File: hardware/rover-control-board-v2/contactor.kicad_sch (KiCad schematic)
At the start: 10 parts, among them Q1 Q_NMOS_DGS

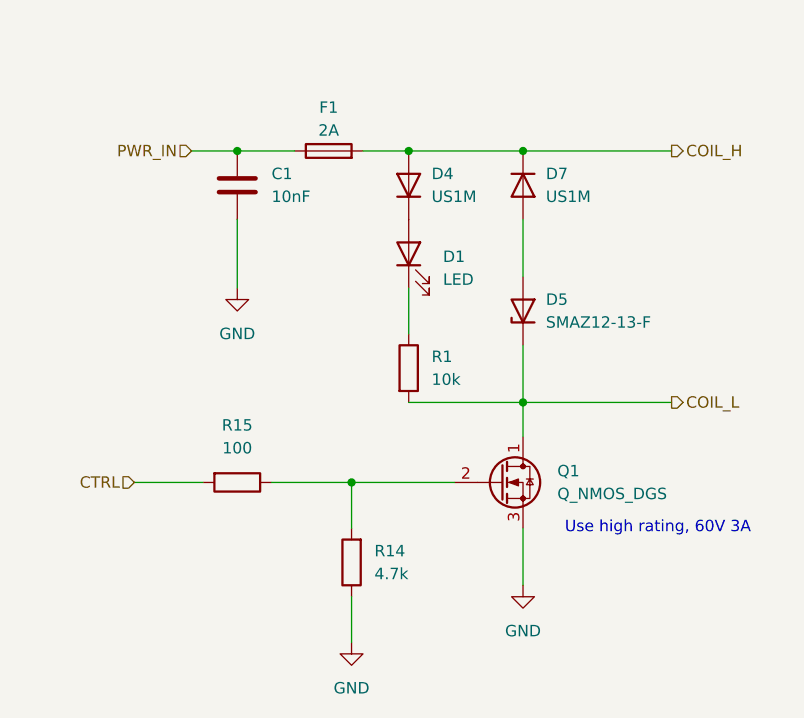
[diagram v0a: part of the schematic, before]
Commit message: Bus routed
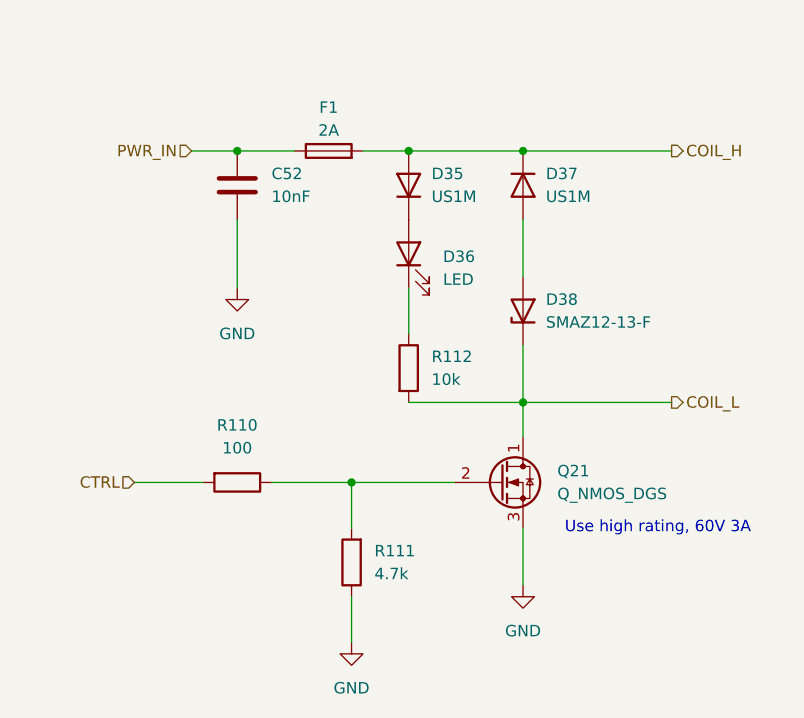
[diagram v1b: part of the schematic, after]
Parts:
- renumbered C1 to C52, D4 to D35, D1 to D36, D7 to D37, D5 to D38, Q1 to Q21, R15 to R110, R14 to R111, R1 to R112
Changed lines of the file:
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@@
 		(dnp no)
 		(fields_autoplaced yes)
-		(property "Reference" "D5"
+		(property "Reference" "D38"
 			(at 91.44 62.2299 90)
 			(show_name no)
@@
 			(project "rover-control-board-v2"
 				(path "/ed12625f-743c-4dd1-a6f4-666aeca01e2d/f186a5df-bce3-4173-b0d9-882f1a8a692c"
-					(reference "D5")
+					(reference "D38")
 					(unit 1)
 				)
@@
 		(dnp no)
 		(fields_autoplaced yes)
-		(property "Reference" "D7"
+		(property "Reference" "D37"
 			(at 91.44 48.2599 90)
 			(show_name no)
@@
 			(project "rover-control-board-v2"
 				(path "/ed12625f-743c-4dd1-a6f4-666aeca01e2d/f186a5df-bce3-4173-b0d9-882f1a8a692c"
-					(reference "D7")
+					(reference "D37")
 					(unit 1)
 				)
@@
 		(dnp no)
 		(fields_autoplaced yes)
-		(property "Reference" "D1"
+		(property "Reference" "D36"
 			(at 80.01 57.4674 90)
 			(show_name no)
@@
 			(project "rover-control-board-v2"
 				(path "/ed12625f-743c-4dd1-a6f4-666aeca01e2d/f186a5df-bce3-4173-b0d9-882f1a8a692c"
-					(reference "D1")
+					(reference "D36")
 					(unit 1)
 				)
@@
 		(dnp no)
 		(fields_autoplaced yes)
-		(property "Reference" "Q1"
+		(property "Reference" "Q21"
 			(at 92.71 81.2799 0)
 			(show_name no)
@@
 			(project "rover-control-board-v2"
 				(path "/ed12625f-743c-4dd1-a6f4-666aeca01e2d/f186a5df-bce3-4173-b0d9-882f1a8a692c"
-					(reference "Q1")
+					(reference "Q21")
 					(unit 1)
 				)
@@
 		(dnp no)
 		(fields_autoplaced yes)
-		(property "Reference" "C1"
+		(property "Reference" "C52"
 			(at 60.96 48.2599 0)
 			(show_name no)
@@
 			(project "rover-control-board-v2"
 				(path "/ed12625f-743c-4dd1-a6f4-666aeca01e2d/f186a5df-bce3-4173-b0d9-882f1a8a692c"
-					(reference "C1")
+					(reference "C52")
 					(unit 1)
 				)
@@
 		(dnp no)
 		(fields_autoplaced yes)
-		(property "Reference" "#PWR04"
+		(property "Reference" "#PWR0152"
 			(at 88.9 100.33 0)
 			(hide yes)
@@
 			(project "rover-control-board-v2"
 				(path "/ed12625f-743c-4dd1-a6f4-666aeca01e2d/f186a5df-bce3-4173-b0d9-882f1a8a692c"
-					(reference "#PWR04")
+					(reference "#PWR0152")
 					(unit 1)
 				)
@@
 		(dnp no)
 		(fields_autoplaced yes)
-		(property "Reference" "D4"
+		(property "Reference" "D35"
 			(at 78.74 48.2599 90)
 			(show_name no)
@@
 			(project "rover-control-board-v2"
 				(path "/ed12625f-743c-4dd1-a6f4-666aeca01e2d/f186a5df-bce3-4173-b0d9-882f1a8a692c"
-					(reference "D4")
+					(reference "D35")
 					(unit 1)
 				)
@@
 		(dnp no)
 		(fields_autoplaced yes)
-		(property "Reference" "#PWR019"
+		(property "Reference" "#PWR0148"
 			(at 13.7086 1.0218 0)
 			(hide yes)
@@
 			(project "rover-control-board-v2"
 				(path "/ed12625f-743c-4dd1-a6f4-666aeca01e2d/f186a5df-bce3-4173-b0d9-882f1a8a692c"
-					(reference "#PWR019")
+					(reference "#PWR0148")
 					(unit 1)
 				)
@@
 		(dnp no)
 		(fields_autoplaced yes)
-		(property "Reference" "#PWR01"
+		(property "Reference" "#PWR0150"
 			(at 57.15 67.31 0)
 			(hide yes)
@@
 			(project "rover-control-board-v2"
 				(path "/ed12625f-743c-4dd1-a6f4-666aeca01e2d/f186a5df-bce3-4173-b0d9-882f1a8a692c"
-					(reference "#PWR01")
+					(reference "#PWR0150")
 					(unit 1)
 				)
@@
 		(dnp no)
 		(fields_autoplaced yes)
-		(property "Reference" "R15"
+		(property "Reference" "R110"
 			(at 57.15 76.2 90)
 			(show_name no)
@@
 			(project "rover-control-board-v2"
 				(path "/ed12625f-743c-4dd1-a6f4-666aeca01e2d/f186a5df-bce3-4173-b0d9-882f1a8a692c"
-					(reference "R15")
+					(reference "R110")
 					(unit 1)
 				)
@@
 		(dnp no)
 		(fields_autoplaced yes)
-		(property "Reference" "R1"
+		(property "Reference" "R112"
 			(at 78.74 68.5799 0)
 			(show_name no)
@@
 			(project "rover-control-board-v2"
 				(path "/ed12625f-743c-4dd1-a6f4-666aeca01e2d/f186a5df-bce3-4173-b0d9-882f1a8a692c"
-					(reference "R1")
+					(reference "R112")
 					(unit 1)
 				)
@@
 		(dnp no)
 		(fields_autoplaced yes)
-		(property "Reference" "R14"
+		(property "Reference" "R111"
 			(at 72.39 90.1699 0)
 			(show_name no)
@@
 			(project "rover-control-board-v2"
 				(path "/ed12625f-743c-4dd1-a6f4-666aeca01e2d/f186a5df-bce3-4173-b0d9-882f1a8a692c"
-					(reference "R14")
+					(reference "R111")
 					(unit 1)
 				)
@@
 		(dnp no)
 		(fields_autoplaced yes)
-		(property "Reference" "#PWR020"
+		(property "Reference" "#PWR0149"
 			(at 16.2486 3.5618 0)
 			(hide yes)
@@
 			(project "rover-control-board-v2"
 				(path "/ed12625f-743c-4dd1-a6f4-666aeca01e2d/f186a5df-bce3-4173-b0d9-882f1a8a692c"
-					(reference "#PWR020")
+					(reference "#PWR0149")
 					(unit 1)
 				)
@@
 		(dnp no)
 		(fields_autoplaced yes)
-		(property "Reference" "#PWR011"
+		(property "Reference" "#PWR0151"
 			(at 69.85 106.68 0)
 			(hide yes)
@@
 			(project "rover-control-board-v2"
 				(path "/ed12625f-743c-4dd1-a6f4-666aeca01e2d/f186a5df-bce3-4173-b0d9-882f1a8a692c"
-					(reference "#PWR011")
-					(unit 1)
-				)
+					(reference "#PWR0151")
+					(unit 1)
+				)

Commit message: revamping channel switches
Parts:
- renumbered C52 to C46, R110 to R109, R111 to R110, R112 to R111
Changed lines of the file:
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@@
 		(dnp no)
 		(fields_autoplaced yes)
-		(property "Reference" "C52"
+		(property "Reference" "C46"
 			(at 60.96 48.2599 0)
 			(show_name no)
@@
 			(project "rover-control-board-v2"
 				(path "/ed12625f-743c-4dd1-a6f4-666aeca01e2d/f186a5df-bce3-4173-b0d9-882f1a8a692c"
-					(reference "C52")
+					(reference "C46")
 					(unit 1)
 				)
@@
 		(dnp no)
 		(fields_autoplaced yes)
-		(property "Reference" "#PWR0152"
+		(property "Reference" "#PWR0146"
 			(at 88.9 100.33 0)
 			(hide yes)
@@
 			(project "rover-control-board-v2"
 				(path "/ed12625f-743c-4dd1-a6f4-666aeca01e2d/f186a5df-bce3-4173-b0d9-882f1a8a692c"
-					(reference "#PWR0152")
+					(reference "#PWR0146")
 					(unit 1)
 				)
@@
 		(dnp no)
 		(fields_autoplaced yes)
-		(property "Reference" "#PWR0148"
+		(property "Reference" "#PWR0142"
 			(at 13.7086 1.0218 0)
 			(hide yes)
@@
 			(project "rover-control-board-v2"
 				(path "/ed12625f-743c-4dd1-a6f4-666aeca01e2d/f186a5df-bce3-4173-b0d9-882f1a8a692c"
-					(reference "#PWR0148")
+					(reference "#PWR0142")
 					(unit 1)
 				)
@@
 		(dnp no)
 		(fields_autoplaced yes)
-		(property "Reference" "#PWR0150"
+		(property "Reference" "#PWR0144"
 			(at 57.15 67.31 0)
 			(hide yes)
@@
 			(project "rover-control-board-v2"
 				(path "/ed12625f-743c-4dd1-a6f4-666aeca01e2d/f186a5df-bce3-4173-b0d9-882f1a8a692c"
-					(reference "#PWR0150")
+					(reference "#PWR0144")
 					(unit 1)
 				)
@@
 		(dnp no)
 		(fields_autoplaced yes)
-		(property "Reference" "R110"
+		(property "Reference" "R109"
 			(at 57.15 76.2 90)
 			(show_name no)
@@
 			(project "rover-control-board-v2"
 				(path "/ed12625f-743c-4dd1-a6f4-666aeca01e2d/f186a5df-bce3-4173-b0d9-882f1a8a692c"
-					(reference "R110")
+					(reference "R109")
 					(unit 1)
 				)
@@
 		(dnp no)
 		(fields_autoplaced yes)
-		(property "Reference" "R112"
+		(property "Reference" "R111"
 			(at 78.74 68.5799 0)
 			(show_name no)
@@
 			(project "rover-control-board-v2"
 				(path "/ed12625f-743c-4dd1-a6f4-666aeca01e2d/f186a5df-bce3-4173-b0d9-882f1a8a692c"
-					(reference "R112")
+					(reference "R111")
 					(unit 1)
 				)
@@
 		(dnp no)
 		(fields_autoplaced yes)
-		(property "Reference" "R111"
+		(property "Reference" "R110"
 			(at 72.39 90.1699 0)
 			(show_name no)
@@
 			(project "rover-control-board-v2"
 				(path "/ed12625f-743c-4dd1-a6f4-666aeca01e2d/f186a5df-bce3-4173-b0d9-882f1a8a692c"
-					(reference "R111")
+					(reference "R110")
 					(unit 1)
 				)
@@
 		(dnp no)
 		(fields_autoplaced yes)
-		(property "Reference" "#PWR0149"
+		(property "Reference" "#PWR0143"
 			(at 16.2486 3.5618 0)
 			(hide yes)
@@
 			(project "rover-control-board-v2"
 				(path "/ed12625f-743c-4dd1-a6f4-666aeca01e2d/f186a5df-bce3-4173-b0d9-882f1a8a692c"
-					(reference "#PWR0149")
+					(reference "#PWR0143")
 					(unit 1)
 				)
@@
 		(dnp no)
 		(fields_autoplaced yes)
-		(property "Reference" "#PWR0151"
+		(property "Reference" "#PWR0145"
 			(at 69.85 106.68 0)
 			(hide yes)
@@
 			(project "rover-control-board-v2"
 				(path "/ed12625f-743c-4dd1-a6f4-666aeca01e2d/f186a5df-bce3-4173-b0d9-882f1a8a692c"
-					(reference "#PWR0151")
-					(unit 1)
-				)
+					(reference "#PWR0145")
+					(unit 1)
+				)

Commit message: Minor fixes and sanity checks
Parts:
- renumbered C46 to C44, D35 to D30, D36 to D31, D37 to D32, D38 to D33, F1 to F7, Q21 to Q27, R109 to R96, R110 to R97, R111 to R98
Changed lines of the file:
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@@
 		(dnp no)
 		(fields_autoplaced yes)
-		(property "Reference" "D38"
+		(property "Reference" "D33"
 			(at 91.44 62.2299 90)
 			(show_name no)
@@
 			(project "rover-control-board-v2"
 				(path "/ed12625f-743c-4dd1-a6f4-666aeca01e2d/f186a5df-bce3-4173-b0d9-882f1a8a692c"
-					(reference "D38")
+					(reference "D33")
 					(unit 1)
 				)
@@
 		(dnp no)
 		(fields_autoplaced yes)
-		(property "Reference" "D37"
+		(property "Reference" "D32"
 			(at 91.44 48.2599 90)
 			(show_name no)
@@
 			(project "rover-control-board-v2"
 				(path "/ed12625f-743c-4dd1-a6f4-666aeca01e2d/f186a5df-bce3-4173-b0d9-882f1a8a692c"
-					(reference "D37")
+					(reference "D32")
 					(unit 1)
 				)
@@
 		(dnp no)
 		(fields_autoplaced yes)
-		(property "Reference" "D36"
+		(property "Reference" "D31"
 			(at 80.01 57.4674 90)
 			(show_name no)
@@
 			(project "rover-control-board-v2"
 				(path "/ed12625f-743c-4dd1-a6f4-666aeca01e2d/f186a5df-bce3-4173-b0d9-882f1a8a692c"
-					(reference "D36")
+					(reference "D31")
 					(unit 1)
 				)
@@
 		(dnp no)
 		(fields_autoplaced yes)
-		(property "Reference" "Q21"
+		(property "Reference" "Q27"
 			(at 92.71 81.2799 0)
 			(show_name no)
@@
 			(project "rover-control-board-v2"
 				(path "/ed12625f-743c-4dd1-a6f4-666aeca01e2d/f186a5df-bce3-4173-b0d9-882f1a8a692c"
-					(reference "Q21")
+					(reference "Q27")
 					(unit 1)
 				)
@@
 		(dnp no)
 		(fields_autoplaced yes)
-		(property "Reference" "C46"
+		(property "Reference" "C44"
 			(at 60.96 48.2599 0)
 			(show_name no)
@@
 			(project "rover-control-board-v2"
 				(path "/ed12625f-743c-4dd1-a6f4-666aeca01e2d/f186a5df-bce3-4173-b0d9-882f1a8a692c"
-					(reference "C46")
+					(reference "C44")
 					(unit 1)
 				)
@@
 		(dnp no)
 		(fields_autoplaced yes)
-		(property "Reference" "#PWR0146"
+		(property "Reference" "#PWR0144"
 			(at 88.9 100.33 0)
 			(hide yes)
@@
 			(project "rover-control-board-v2"
 				(path "/ed12625f-743c-4dd1-a6f4-666aeca01e2d/f186a5df-bce3-4173-b0d9-882f1a8a692c"
-					(reference "#PWR0146")
+					(reference "#PWR0144")
 					(unit 1)
 				)
@@
 		(dnp no)
 		(fields_autoplaced yes)
-		(property "Reference" "D35"
+		(property "Reference" "D30"
 			(at 78.74 48.2599 90)
 			(show_name no)
@@
 			(project "rover-control-board-v2"
 				(path "/ed12625f-743c-4dd1-a6f4-666aeca01e2d/f186a5df-bce3-4173-b0d9-882f1a8a692c"
-					(reference "D35")
+					(reference "D30")
 					(unit 1)
 				)
@@
 		(dnp no)
 		(fields_autoplaced yes)
-		(property "Reference" "#PWR0142"
+		(property "Reference" "#PWR0140"
 			(at 13.7086 1.0218 0)
 			(hide yes)
@@
 			(project "rover-control-board-v2"
 				(path "/ed12625f-743c-4dd1-a6f4-666aeca01e2d/f186a5df-bce3-4173-b0d9-882f1a8a692c"
-					(reference "#PWR0142")
+					(reference "#PWR0140")
 					(unit 1)
 				)
@@
 		(dnp no)
 		(fields_autoplaced yes)
-		(property "Reference" "#PWR0144"
+		(property "Reference" "#PWR0142"
 			(at 57.15 67.31 0)
 			(hide yes)
@@
 			(project "rover-control-board-v2"
 				(path "/ed12625f-743c-4dd1-a6f4-666aeca01e2d/f186a5df-bce3-4173-b0d9-882f1a8a692c"
-					(reference "#PWR0144")
+					(reference "#PWR0142")
 					(unit 1)
 				)
@@
 		(dnp no)
 		(fields_autoplaced yes)
-		(property "Reference" "R109"
+		(property "Reference" "R96"
 			(at 57.15 76.2 90)
 			(show_name no)
@@
 			(project "rover-control-board-v2"
 				(path "/ed12625f-743c-4dd1-a6f4-666aeca01e2d/f186a5df-bce3-4173-b0d9-882f1a8a692c"
-					(reference "R109")
+					(reference "R96")
 					(unit 1)
 				)
@@
 		(dnp no)
 		(fields_autoplaced yes)
-		(property "Reference" "R111"
+		(property "Reference" "R98"
 			(at 78.74 68.5799 0)
 			(show_name no)
@@
 			(project "rover-control-board-v2"
 				(path "/ed12625f-743c-4dd1-a6f4-666aeca01e2d/f186a5df-bce3-4173-b0d9-882f1a8a692c"
-					(reference "R111")
+					(reference "R98")
 					(unit 1)
 				)
@@
 		(in_pos_files yes)
 		(dnp no)
-		(property "Reference" "F1"
+		(property "Reference" "F7"
 			(at 67.31 40.894 90)
 			(show_name no)
@@
 			(project "rover-control-board-v2"
 				(path "/ed12625f-743c-4dd1-a6f4-666aeca01e2d/f186a5df-bce3-4173-b0d9-882f1a8a692c"
-					(reference "F1")
+					(reference "F7")
 					(unit 1)
 				)
@@
 		(dnp no)
 		(fields_autoplaced yes)
-		(property "Reference" "R110"
+		(property "Reference" "R97"
 			(at 72.39 90.1699 0)
 			(show_name no)
@@
 			(project "rover-control-board-v2"
 				(path "/ed12625f-743c-4dd1-a6f4-666aeca01e2d/f186a5df-bce3-4173-b0d9-882f1a8a692c"
-					(reference "R110")
+					(reference "R97")
 					(unit 1)
 				)
@@
 		(dnp no)
 		(fields_autoplaced yes)
-		(property "Reference" "#PWR0143"
+		(property "Reference" "#PWR0141"
 			(at 16.2486 3.5618 0)
 			(hide yes)
@@
 			(project "rover-control-board-v2"
 				(path "/ed12625f-743c-4dd1-a6f4-666aeca01e2d/f186a5df-bce3-4173-b0d9-882f1a8a692c"
-					(reference "#PWR0143")
+					(reference "#PWR0141")
 					(unit 1)
 				)
@@
 		(dnp no)
 		(fields_autoplaced yes)
-		(property "Reference" "#PWR0145"
+		(property "Reference" "#PWR0143"
 			(at 69.85 106.68 0)
 			(hide yes)
@@
 			(project "rover-control-board-v2"
 				(path "/ed12625f-743c-4dd1-a6f4-666aeca01e2d/f186a5df-bce3-4173-b0d9-882f1a8a692c"
-					(reference "#PWR0145")
-					(unit 1)
-				)
+					(reference "#PWR0143")
+					(unit 1)
+				)

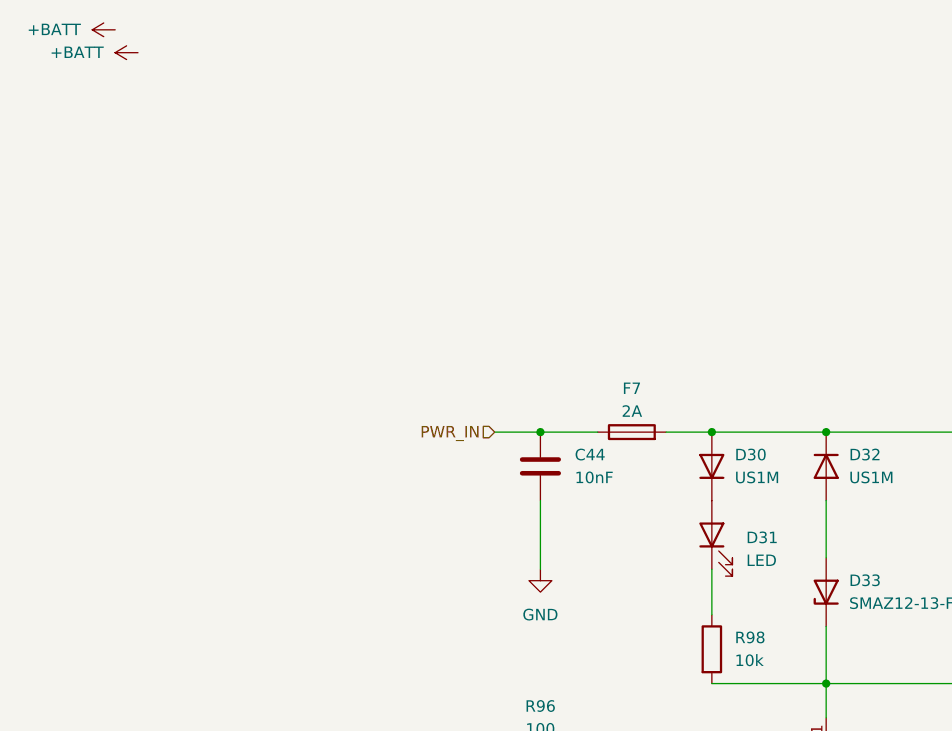
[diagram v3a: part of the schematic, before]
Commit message: Added photovoltaic gate driver and ESD protection
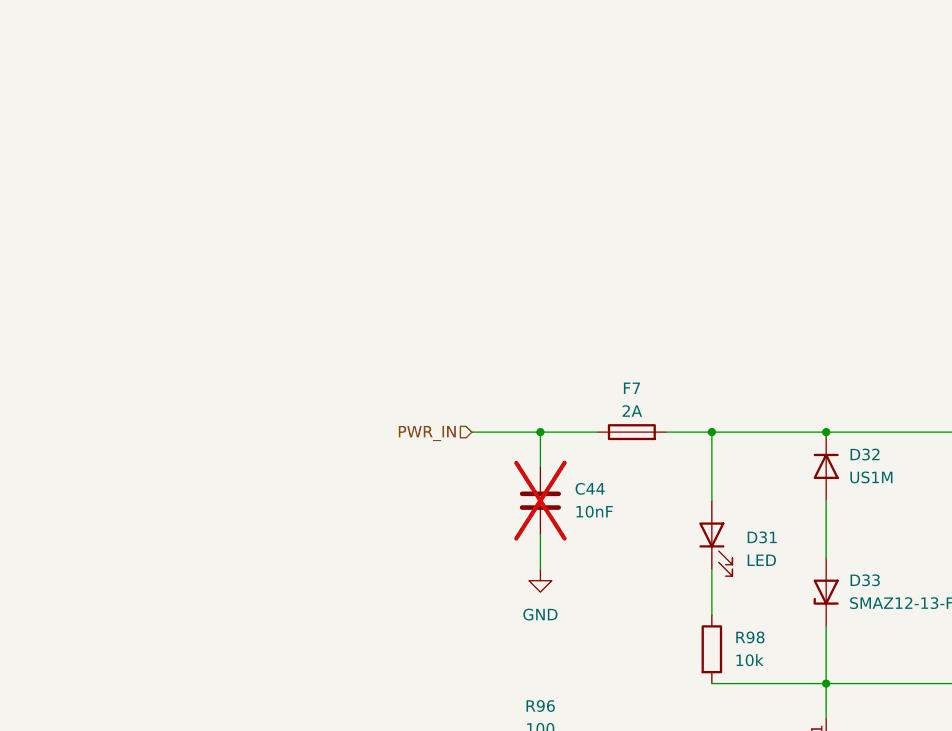
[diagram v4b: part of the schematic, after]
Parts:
- removed D30: US1M, Diode_SMD:D_SMA, symbol Diode:US1M
- C44: now not fitted
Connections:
- net COIL_H: now also D31.2 (A)
